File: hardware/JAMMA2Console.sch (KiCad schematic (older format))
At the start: 30 parts, among them J1 Conn_02x28_JAMMA, J2 DB15_Female_HighDensity, J3 SCART-F, J4 DF1BZ-34DP-2.5DSA, J5 Conn_Coaxial_x2, J6 DB15_Female, J7 DB15_Female, J8 Phoenix PTS 1,5/4-5.0, J9 USB_B, U1 USBLC6-2P6, U2 LD1117-3.3

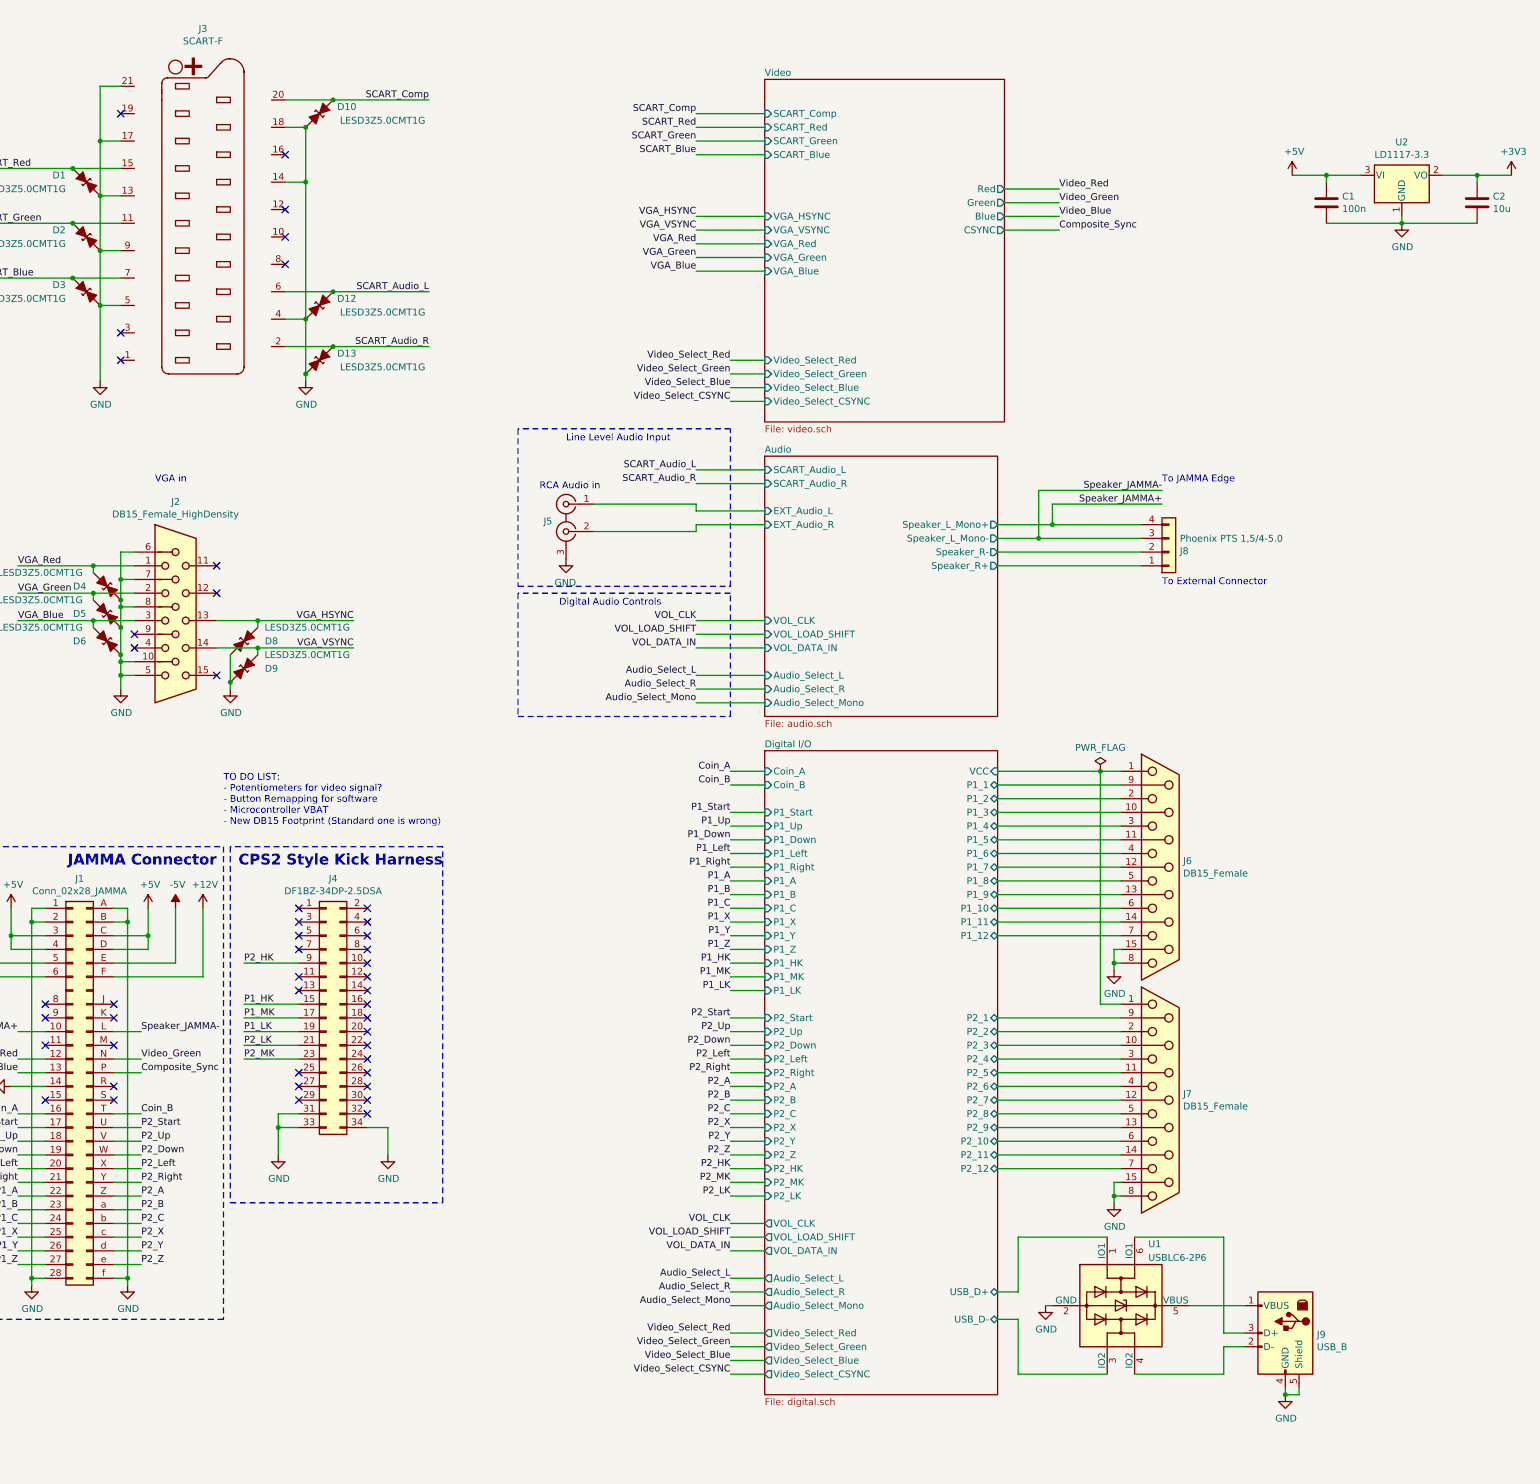
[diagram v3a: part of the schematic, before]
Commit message: Completing the functionality of PCB layout. Require silkscreen placement still, though.
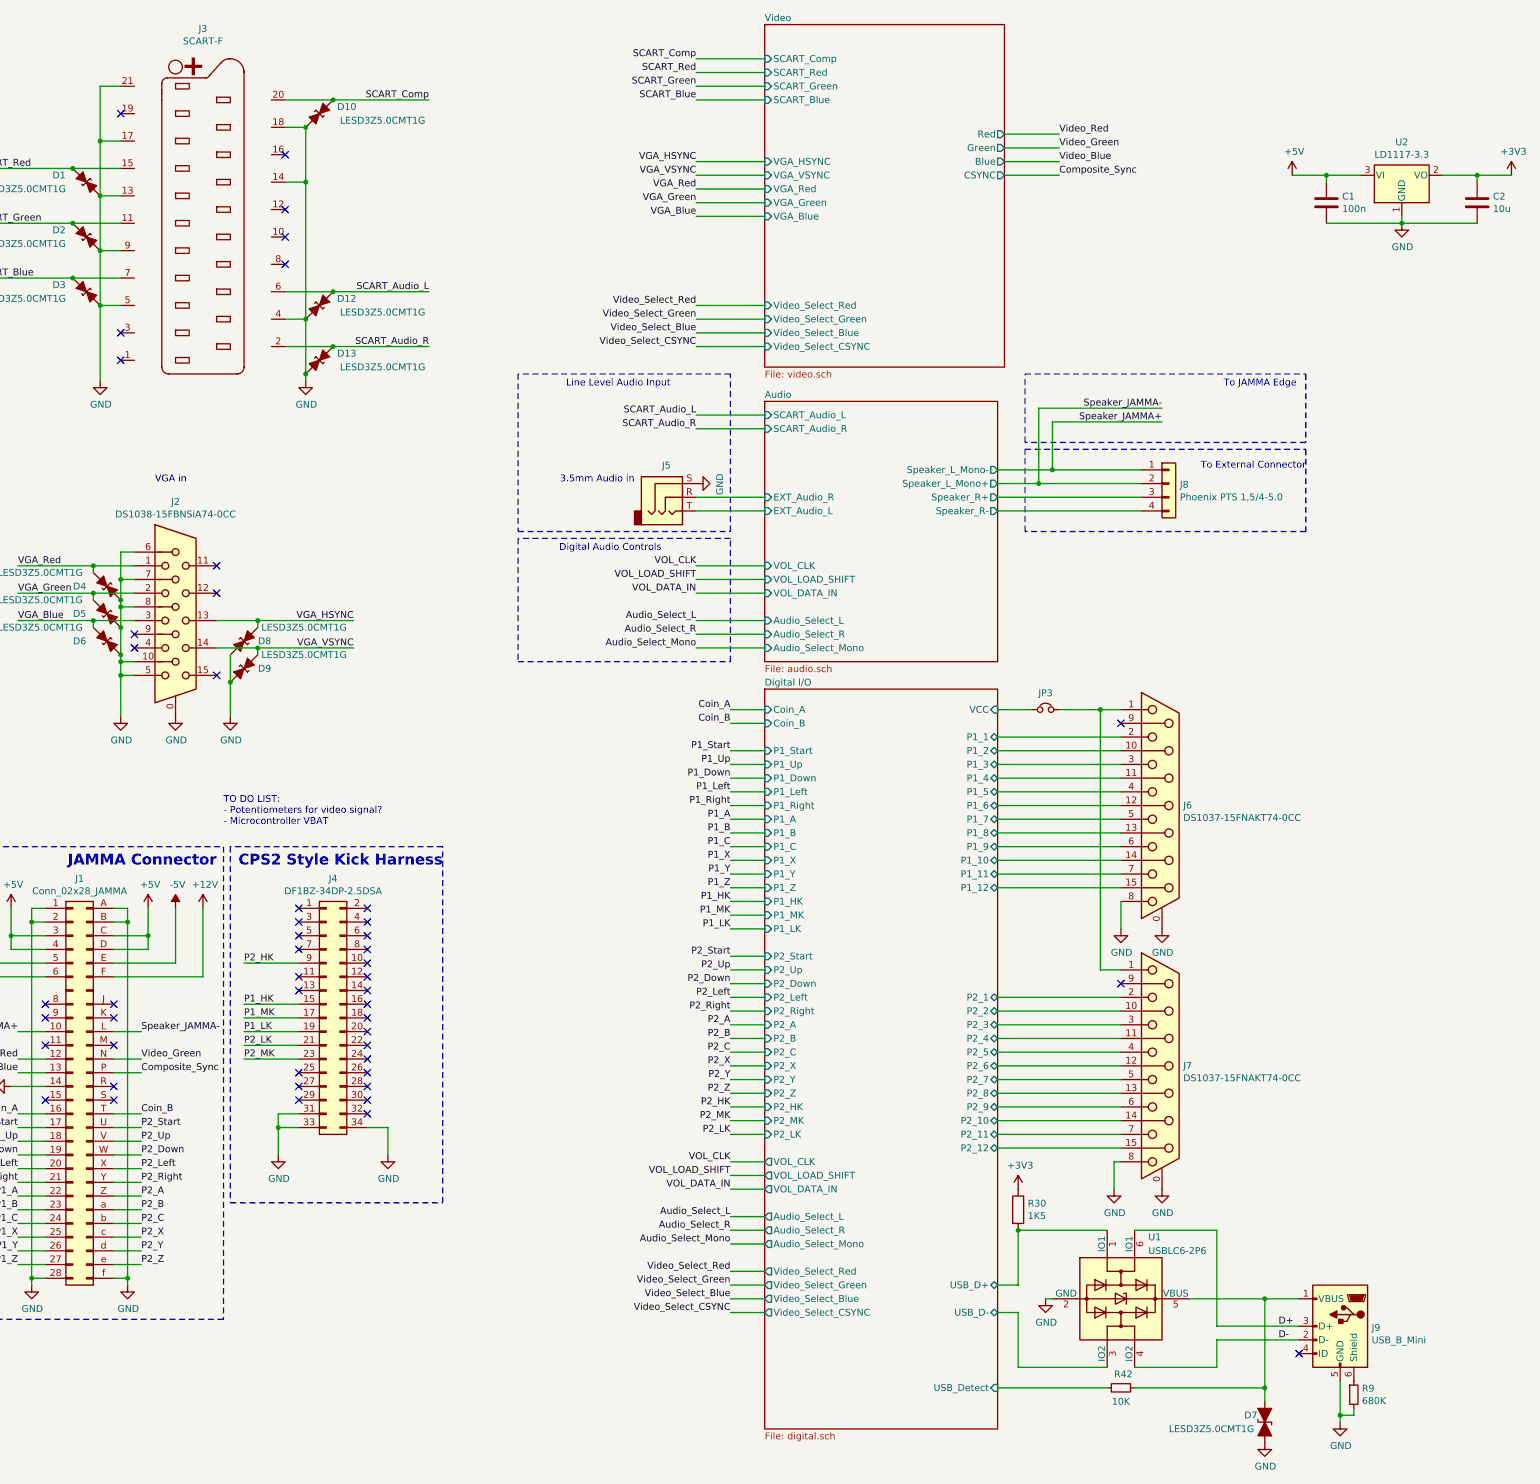
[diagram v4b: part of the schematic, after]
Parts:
- removed J2: DB15_Female_HighDensity, Connector_Dsub:DSUB-15-HD_Female_Horizontal_P2.29x1.98mm_EdgePinOffset8.35mm_Housed_MountingHolesOffset10.89mm, symbol Connector:DB15_Female_HighDensity
- removed J5: Conn_Coaxial_x2, Console2JAMMA:RCA_Switchchraft_Dual, symbol Connector:Conn_Coaxial_x2
- removed J6, J7: DB15_Female, Connector_Dsub:DSUB-15_Female_Horizontal_P2.77x2.84mm_EdgePinOffset7.70mm_Housed_MountingHolesOffset9.12mm, symbol Connector:DB15_Female
- removed J9: USB_B, Connector_USB:USB_B_OST_USB-B1HSxx_Horizontal, symbol Connector:USB_B
- added D7: LESD3Z5.0CMT1G, Diode_SMD:D_SOD-323, symbol Device:D_TVS_ALT
- added J2: DS1038-15FBNSiA74-0CC, Console2JAMMA:DSUB-15-HD_Female_Horizontal_P2.29x1.98mm_EdgePinOffset8.63mm_Housed_MountingHolesOffset11.17mm, symbol Connector:DB15_Female_HighDensity_MountingHoles
- added J5: AudioJack3, Connector_Audio:Jack_3.5mm_CUI_SJ-3523-SMT_Horizontal, symbol Connector:AudioJack3
- added J6, J7: DS1037-15FNAKT74-0CC, Console2JAMMA:DSUB-15_Female_Horizontal_P2.77x2.84mm_EdgePinOffset8.10mm_Housed_MountingHolesOffset9.52mm, symbol Connector:DB15_Female_MountingHoles
- added J9: USB_B_Mini, Connector_USB:USB_Mini-B_Lumberg_2486_01_Horizontal, symbol Connector:USB_B_Mini
- added JP3: Jumper_NC_Small, Jumper:SolderJumper-2_P1.3mm_Bridged2Bar_Pad1.0x1.5mm, symbol Device:Jumper_NC_Small
- added R30: 1K5, Resistor_SMD:R_0603_1608Metric, symbol Device:R
- added R42: 10K, Resistor_SMD:R_0603_1608Metric, symbol Device:R_Small
- added R9: 680K, Resistor_SMD:R_0603_1608Metric, symbol Device:R_Small
- J3: footprint Console2JAMMA:Conn_SCART_Female -> Console2JAMMA:Conn_SCART_Female_Right_Angle
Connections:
- net +3V3: now also R30.1
- net Audio/EXT_Audio_L: now also J5.T
- net Audio/EXT_Audio_R: now also J5.R
- net Audio/Speaker_R+: now also J8.3 (Pin_3); no longer J8.1 (Pin_1)
- net Audio/Speaker_R-: now also J8.4 (Pin_4); no longer J8.2 (Pin_2)
- net Digital I/O/P1_1: now also J6.2
- net Digital I/O/P1_10: now also J6.14 (P14)
- net Digital I/O/P1_11: now also J6.7
- net Digital I/O/P1_12: now also J6.15 (P15)
- net Digital I/O/P1_2: now also J6.10 (P10)
- net Digital I/O/P1_3: now also J6.3
- net Digital I/O/P1_4: now also J6.11 (P111)
- net Digital I/O/P1_5: now also J6.4
- net Digital I/O/P1_6: now also J6.12 (P12)
- net Digital I/O/P1_7: now also J6.5
- net Digital I/O/P1_8: now also J6.13 (P13)
- net Digital I/O/P1_9: now also J6.6
- net Digital I/O/P2_1: now also J7.2
- net Digital I/O/P2_10: now also J7.14 (P14)
- net Digital I/O/P2_11: now also J7.7
- net Digital I/O/P2_12: now also J7.15 (P15)
- net Digital I/O/P2_2: now also J7.10 (P10)
- net Digital I/O/P2_3: now also J7.3
- net Digital I/O/P2_4: now also J7.11 (P111)
- net Digital I/O/P2_5: now also J7.4
- net Digital I/O/P2_6: now also J7.12 (P12)
- net Digital I/O/P2_7: now also J7.5
- net Digital I/O/P2_8: now also J7.13 (P13)
- net Digital I/O/P2_9: now also J7.6
- net Digital I/O/USB_D+: now also R30.2
- net Digital I/O/VCC: now also JP3.1
- net GND: now also D8.1, D9.1, D7.2 (A2), J2.0, J2.10, J2.5, J2.6, J2.7, J2.8, J5.S, J6.0 (PAD), J6.8, J7.0 (PAD), J7.8, J9.5 (GND), R9.2; no longer D8.2, D9.2
- net Speaker_JAMMA+: now also J8.1 (Pin_1); no longer J8.4 (Pin_4)
- net Speaker_JAMMA-: now also J8.2 (Pin_2); no longer J8.3 (Pin_3)
- net VGA_Blue: now also J2.3
- net VGA_Green: now also J2.2
- net VGA_HSYNC: now also D8.2, J2.13; no longer D8.1
- net VGA_Red: now also J2.1
- net VGA_VSYNC: now also D9.2, J2.14; no longer D9.1
- net at U1.5 (VBUS): now also D7.1 (A1), J9.1 (VBUS), R42.1
- net D-: now reaches U1.4 (IO2)
- net D-: now also J9.2 (D-)
- net D+: now reaches U1.6 (IO1)
- net D+: now also J9.3 (D+)
- new net: J6.1, J7.1, JP3.2
- new net: J9.6 (Shield), R9.1
- new net Digital I/O/USB_Detect: R42.2
- no-connect marks 46 -> 49
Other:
- note added: "3.5mm Audio in"
- note added: "TO DO LIST:\n- Potentiometers for video signal?\n- Microcontroller VBAT\n"
- note removed: "RCA Audio in"
- note removed: "TO DO LIST:\n- Potentiometers for video signal?\n- Button Remapping for software\n- Microcontroller VBAT\n- New DB15 Footprint (Standard one is wrong)\n"
- moved on the sheet: J8, U1
